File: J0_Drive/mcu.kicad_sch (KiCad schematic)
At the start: 1 part, among them U2 STM32G431RBTx

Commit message: started connecting root
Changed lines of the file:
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@@
 	(generator_version "10.0")
 	(paper "A4")
+	(wire
+		(pts
+			(xy 30.48 34.29) (xy 38.1 34.29)
+		)
+		(stroke
+			(width 0)
+			(type default)
+		)
+	)
+	(wire
+		(pts
+			(xy 30.48 39.37) (xy 38.1 39.37)
+		)
+		(stroke
+			(width 0)
+			(type default)
+		)
+	)
+	(wire
+		(pts
+			(xy 30.48 24.13) (xy 38.1 24.13)
+		)
+		(stroke
+			(width 0)
+			(type default)
+		)
+	)
+	(wire
+		(pts
+			(xy 30.48 21.59) (xy 38.1 21.59)
+		)
+		(stroke
+			(width 0)
+			(type default)
+		)
+	)
+	(wire
+		(pts
+			(xy 30.48 44.45) (xy 38.1 44.45)
+		)
+		(stroke
+			(width 0)
+			(type default)
+		)
+	)
+	(wire
+		(pts
+			(xy 30.48 46.99) (xy 38.1 46.99)
+		)
+		(stroke
+			(width 0)
+			(type default)
+		)
+	)
+	(wire
+		(pts
+			(xy 30.48 26.67) (xy 38.1 26.67)
+		)
+		(stroke
+			(width 0)
+			(type default)
+		)
+	)
+	(wire
+		(pts
+			(xy 30.48 31.75) (xy 38.1 31.75)
+		)
+		(stroke
+			(width 0)
+			(type default)
+		)
+	)
+	(wire
+		(pts
+			(xy 30.48 49.53) (xy 38.1 49.53)
+		)
+		(stroke
+			(width 0)
+			(type default)
+		)
+	)
+	(wire
+		(pts
+			(xy 30.48 29.21) (xy 38.1 29.21)
+		)
+		(stroke
+			(width 0)
+			(type default)
+		)
+	)
+	(label "ISENSE_C"
+		(at 38.1 49.53 0)
+		(effects
+			(font
+				(size 1.27 1.27)
+			)
+			(justify left bottom)
+		)
+	)
+	(label "INH3{slash}IN3"
+		(at 38.1 31.75 0)
+		(effects
+			(font
+				(size 1.27 1.27)
+			)
+			(justify left bottom)
+		)
+	)
+	(label "nFAULT"
+		(at 38.1 39.37 0)
+		(effects
+			(font
+				(size 1.27 1.27)
+			)
+			(justify left bottom)
+		)
+	)
+	(label "ISENSE_A"
+		(at 38.1 44.45 0)
+		(effects
+			(font
+				(size 1.27 1.27)
+			)
+			(justify left bottom)
+		)
+	)
+	(label "INH2{slash}IN2"
+		(at 38.1 26.67 0)
+		(effects
+			(font
+				(size 1.27 1.27)
+			)
+			(justify left bottom)
+		)
+	)
+	(label "INL1{slash}EN1"
+		(at 38.1 24.13 0)
+		(effects
+			(font
+				(size 1.27 1.27)
+			)
+			(justify left bottom)
+		)
+	)
+	(label "INH1{slash}IN1"
+		(at 38.1 21.59 0)
+		(effects
+			(font
+				(size 1.27 1.27)
+			)
+			(justify left bottom)
+		)
+	)
+	(label "INL2{slash}EN2"
+		(at 38.1 29.21 0)
+		(effects
+			(font
+				(size 1.27 1.27)
+			)
+			(justify left bottom)
+		)
+	)
+	(label "INL3{slash}EN3"
+		(at 38.1 34.29 0)
+		(effects
+			(font
+				(size 1.27 1.27)
+			)
+			(justify left bottom)
+		)
+	)
+	(label "ISENSE_B"
+		(at 38.1 46.99 0)
+		(effects
+			(font
+				(size 1.27 1.27)
+			)
+			(justify left bottom)
+		)
+	)
+	(hierarchical_label "ISENSE_A"
+		(shape input)
+		(at 30.48 44.45 180)
+		(effects
+			(font
+				(size 1.27 1.27)
+			)
+			(justify right)
+		)
+	)
 	(hierarchical_label "INL1{slash}EN1"
 		(shape output)
-		(at 105.41 82.55 180)
+		(at 30.48 24.13 180)
 		(effects
 			(font
@@
 	(hierarchical_label "nFAULT"
 		(shape input)
-		(at 102.87 101.6 180)
+		(at 30.48 39.37 180)
 		(effects
 			(font
@@
 	(hierarchical_label "INL3{slash}EN3"
 		(shape output)
-		(at 105.41 87.63 180)
+		(at 30.48 34.29 180)
+		(effects
+			(font
+				(size 1.27 1.27)
+			)
+			(justify right)
+		)
+	)
+	(hierarchical_label "ISENSE_C"
+		(shape input)
+		(at 30.48 49.53 180)
 		(effects
 			(font
@@
 	(hierarchical_label "INH3{slash}IN3"
 		(shape output)
-		(at 105.41 80.01 180)
+		(at 30.48 31.75 180)
 		(effects
 			(font
@@
 	(hierarchical_label "INH1{slash}IN1"
 		(shape output)
-		(at 105.41 74.93 180)
+		(at 30.48 21.59 180)
 		(effects
 			(font
@@
 	(hierarchical_label "INL2{slash}EN2"
 		(shape output)
-		(at 105.41 85.09 180)
+		(at 30.48 29.21 180)
+		(effects
+			(font
+				(size 1.27 1.27)
+			)
+			(justify right)
+		)
+	)
+	(hierarchical_label "ISENSE_B"
+		(shape input)
+		(at 30.48 46.99 180)
 		(effects
 			(font
@@
 	(hierarchical_label "INH2{slash}IN2"
 		(shape output)
-		(at 105.41 77.47 180)
-		(effects
-			(font
+		(at 30.48 26.67 180)
+		(effects
+			(font

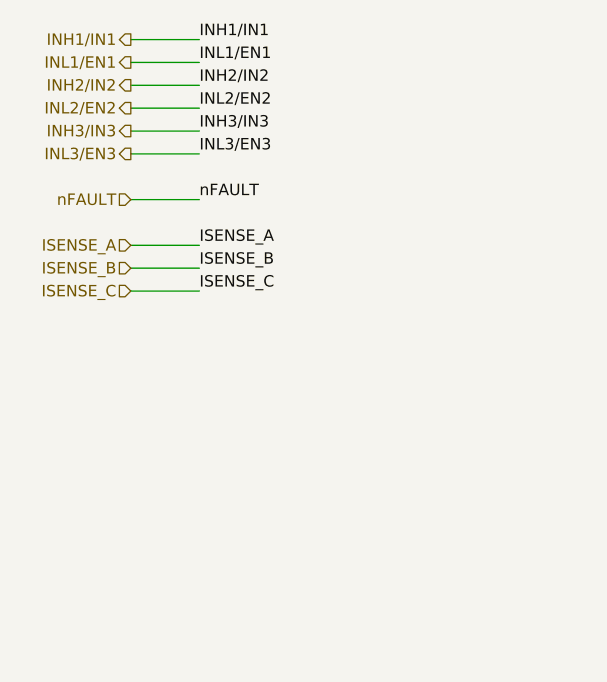
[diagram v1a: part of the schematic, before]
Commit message: organized hierarchical sheets, finished communications, started sensors
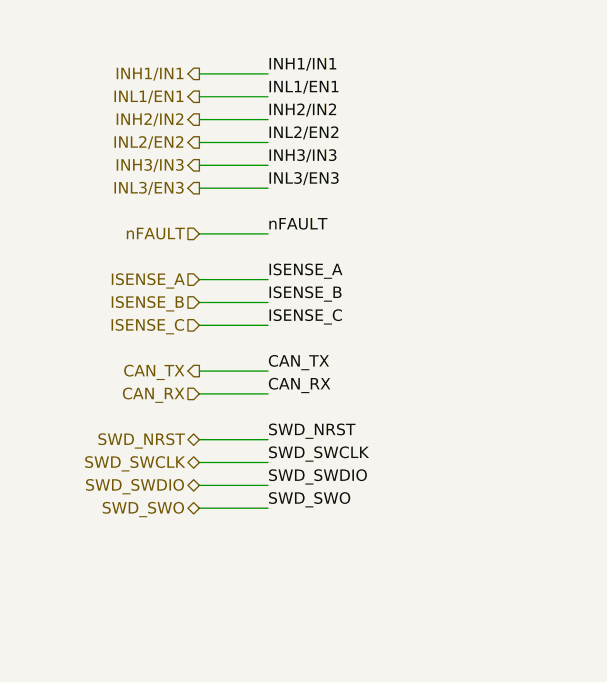
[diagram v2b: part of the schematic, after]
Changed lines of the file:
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@@
 	(wire
 		(pts
-			(xy 30.48 34.29) (xy 38.1 34.29)
-		)
-		(stroke
-			(width 0)
-			(type default)
-		)
-	)
-	(wire
-		(pts
-			(xy 30.48 39.37) (xy 38.1 39.37)
-		)
-		(stroke
-			(width 0)
-			(type default)
-		)
-	)
-	(wire
-		(pts
-			(xy 30.48 24.13) (xy 38.1 24.13)
-		)
-		(stroke
-			(width 0)
-			(type default)
-		)
-	)
-	(wire
-		(pts
-			(xy 30.48 21.59) (xy 38.1 21.59)
-		)
-		(stroke
-			(width 0)
-			(type default)
-		)
-	)
-	(wire
-		(pts
-			(xy 30.48 44.45) (xy 38.1 44.45)
-		)
-		(stroke
-			(width 0)
-			(type default)
-		)
-	)
-	(wire
-		(pts
-			(xy 30.48 46.99) (xy 38.1 46.99)
-		)
-		(stroke
-			(width 0)
-			(type default)
-		)
-	)
-	(wire
-		(pts
-			(xy 30.48 26.67) (xy 38.1 26.67)
-		)
-		(stroke
-			(width 0)
-			(type default)
-		)
-	)
-	(wire
-		(pts
-			(xy 30.48 31.75) (xy 38.1 31.75)
-		)
-		(stroke
-			(width 0)
-			(type default)
-		)
-	)
-	(wire
-		(pts
-			(xy 30.48 49.53) (xy 38.1 49.53)
-		)
-		(stroke
-			(width 0)
-			(type default)
-		)
-	)
-	(wire
-		(pts
-			(xy 30.48 29.21) (xy 38.1 29.21)
+			(xy 38.1 38.1) (xy 45.72 38.1)
+		)
+		(stroke
+			(width 0)
+			(type default)
+		)
+	)
+	(wire
+		(pts
+			(xy 38.1 43.18) (xy 45.72 43.18)
+		)
+		(stroke
+			(width 0)
+			(type default)
+		)
+	)
+	(wire
+		(pts
+			(xy 38.1 68.58) (xy 45.72 68.58)
+		)
+		(stroke
+			(width 0)
+			(type default)
+		)
+	)
+	(wire
+		(pts
+			(xy 38.1 66.04) (xy 45.72 66.04)
+		)
+		(stroke
+			(width 0)
+			(type default)
+		)
+	)
+	(wire
+		(pts
+			(xy 38.1 60.96) (xy 45.72 60.96)
+		)
+		(stroke
+			(width 0)
+			(type default)
+		)
+	)
+	(wire
+		(pts
+			(xy 38.1 73.66) (xy 45.72 73.66)
+		)
+		(stroke
+			(width 0)
+			(type default)
+		)
+	)
+	(wire
+		(pts
+			(xy 38.1 27.94) (xy 45.72 27.94)
+		)
+		(stroke
+			(width 0)
+			(type default)
+		)
+	)
+	(wire
+		(pts
+			(xy 38.1 25.4) (xy 45.72 25.4)
+		)
+		(stroke
+			(width 0)
+			(type default)
+		)
+	)
+	(wire
+		(pts
+			(xy 38.1 48.26) (xy 45.72 48.26)
+		)
+		(stroke
+			(width 0)
+			(type default)
+		)
+	)
+	(wire
+		(pts
+			(xy 38.1 50.8) (xy 45.72 50.8)
+		)
+		(stroke
+			(width 0)
+			(type default)
+		)
+	)
+	(wire
+		(pts
+			(xy 38.1 30.48) (xy 45.72 30.48)
+		)
+		(stroke
+			(width 0)
+			(type default)
+		)
+	)
+	(wire
+		(pts
+			(xy 38.1 71.12) (xy 45.72 71.12)
+		)
+		(stroke
+			(width 0)
+			(type default)
+		)
+	)
+	(wire
+		(pts
+			(xy 38.1 35.56) (xy 45.72 35.56)
+		)
+		(stroke
+			(width 0)
+			(type default)
+		)
+	)
+	(wire
+		(pts
+			(xy 38.1 53.34) (xy 45.72 53.34)
+		)
+		(stroke
+			(width 0)
+			(type default)
+		)
+	)
+	(wire
+		(pts
+			(xy 38.1 58.42) (xy 45.72 58.42)
+		)
+		(stroke
+			(width 0)
+			(type default)
+		)
+	)
+	(wire
+		(pts
+			(xy 38.1 33.02) (xy 45.72 33.02)
 		)
 		(stroke
@@
 	)
 	(label "ISENSE_C"
-		(at 38.1 49.53 0)
+		(at 45.72 53.34 0)
+		(effects
+			(font
+				(size 1.27 1.27)
+			)
+			(justify left bottom)
+		)
+	)
+	(label "SWD_SWDIO"
+		(at 45.72 71.12 0)
 		(effects
 			(font
@@
 	)
 	(label "INH3{slash}IN3"
-		(at 38.1 31.75 0)
+		(at 45.72 35.56 0)
+		(effects
+			(font
+				(size 1.27 1.27)
+			)
+			(justify left bottom)
+		)
+	)
+	(label "SWD_SWO"
+		(at 45.72 73.66 0)
+		(effects
+			(font
+				(size 1.27 1.27)
+			)
+			(justify left bottom)
+		)
+	)
+	(label "CAN_RX"
+		(at 45.72 60.96 0)
 		(effects
 			(font
@@
 	)
 	(label "nFAULT"
-		(at 38.1 39.37 0)
+		(at 45.72 43.18 0)
 		(effects
 			(font
@@
 	)
 	(label "ISENSE_A"
-		(at 38.1 44.45 0)
+		(at 45.72 48.26 0)
 		(effects
 			(font
@@
 	)
 	(label "INH2{slash}IN2"
-		(at 38.1 26.67 0)
+		(at 45.72 30.48 0)
 		(effects
 			(font
@@
 	)
 	(label "INL1{slash}EN1"
-		(at 38.1 24.13 0)
+		(at 45.72 27.94 0)
 		(effects
 			(font
@@
 	)
 	(label "INH1{slash}IN1"
-		(at 38.1 21.59 0)
+		(at 45.72 25.4 0)
 		(effects
 			(font
@@
 	)
 	(label "INL2{slash}EN2"
-		(at 38.1 29.21 0)
+		(at 45.72 33.02 0)
+		(effects
+			(font
+				(size 1.27 1.27)
+			)
+			(justify left bottom)
+		)
+	)
+	(label "CAN_TX"
+		(at 45.72 58.42 0)
 		(effects
 			(font
@@
 	)
 	(label "INL3{slash}EN3"
-		(at 38.1 34.29 0)
+		(at 45.72 38.1 0)
+		(effects
+			(font
+				(size 1.27 1.27)
+			)
+			(justify left bottom)
+		)
+	)
+	(label "SWD_SWCLK"
+		(at 45.72 68.58 0)
 		(effects
 			(font
@@
 	)
 	(label "ISENSE_B"
-		(at 38.1 46.99 0)
+		(at 45.72 50.8 0)
+		(effects
+			(font
+				(size 1.27 1.27)
+			)
+			(justify left bottom)
+		)
+	)
+	(label "SWD_NRST"
+		(at 45.72 66.04 0)
 		(effects
 			(font
@@
 	(hierarchical_label "ISENSE_A"
 		(shape input)
-		(at 30.48 44.45 180)
+		(at 38.1 48.26 180)
+		(effects
+			(font
+				(size 1.27 1.27)
+			)
+			(justify right)
+		)
+	)
+	(hierarchical_label "SWD_SWDIO"
+		(shape bidirectional)
+		(at 38.1 71.12 180)
 		(effects
 			(font
@@
 	(hierarchical_label "INL1{slash}EN1"
 		(shape output)
-		(at 30.48 24.13 180)
+		(at 38.1 27.94 180)
+		(effects
+			(font
+				(size 1.27 1.27)
+			)
+			(justify right)
+		)
+	)
+	(hierarchical_label "SWD_SWO"
+		(shape bidirectional)
+		(at 38.1 73.66 180)
 		(effects
 			(font
@@
 	(hierarchical_label "nFAULT"
 		(shape input)
-		(at 30.48 39.37 180)
+		(at 38.1 43.18 180)
+		(effects
+			(font
+				(size 1.27 1.27)
+			)
+			(justify right)
+		)
+	)
+	(hierarchical_label "CAN_TX"
+		(shape output)
+		(at 38.1 58.42 180)
 		(effects
 			(font
@@
 	(hierarchical_label "INL3{slash}EN3"
 		(shape output)
-		(at 30.48 34.29 180)
+		(at 38.1 38.1 180)
 		(effects
 			(font
@@
 	(hierarchical_label "ISENSE_C"
 		(shape input)
-		(at 30.48 49.53 180)
+		(at 38.1 53.34 180)
+		(effects
+			(font
+				(size 1.27 1.27)
+			)
+			(justify right)
+		)
+	)
+	(hierarchical_label "CAN_RX"
+		(shape input)
+		(at 38.1 60.96 180)
+		(effects
+			(font
+				(size 1.27 1.27)
+			)
+			(justify right)
+		)
+	)
+	(hierarchical_label "SWD_SWCLK"
+		(shape bidirectional)
+		(at 38.1 68.58 180)
 		(effects
 			(font
@@
 	(hierarchical_label "INH3{slash}IN3"
 		(shape output)
-		(at 30.48 31.75 180)
+		(at 38.1 35.56 180)
 		(effects
 			(font
@@
 	(hierarchical_label "INH1{slash}IN1"
 		(shape output)
-		(at 30.48 21.59 180)
+		(at 38.1 25.4 180)
 		(effects
 			(font
@@
 	(hierarchical_label "INL2{slash}EN2"
 		(shape output)
-		(at 30.48 29.21 180)
+		(at 38.1 33.02 180)
+		(effects
+			(font
+				(size 1.27 1.27)
+			)
+			(justify right)
+		)
+	)
+	(hierarchical_label "SWD_NRST"
+		(shape bidirectional)
+		(at 38.1 66.04 180)
 		(effects
 			(font
@@
 	(hierarchical_label "ISENSE_B"
 		(shape input)
-		(at 30.48 46.99 180)
+		(at 38.1 50.8 180)
 		(effects
 			(font
@@
 	(hierarchical_label "INH2{slash}IN2"
 		(shape output)
-		(at 30.48 26.67 180)
-		(effects
-			(font
+		(at 38.1 30.48 180)
+		(effects
+			(font

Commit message: started misc page, added test points, mounting holes, fiducials, etc.
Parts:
- added U8: LM5164DDA, Package_SO:HSOP-8-1EP_3.9x4.9mm_P1.27mm_EP2.41x3.1mm_ThermalVias, symbol Regulator_Switching:LM5164DDA
- added U9: TLV75533PDBV, Package_TO_SOT_SMD:SOT-23-5, symbol Regulator_Linear:TLV75533PDBV
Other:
- note added: "(follow typical application)"
- note added: "3.3V Regulator"
- note added: "5V Buck"
- note added: "5V to 3.3V"
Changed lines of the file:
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@@
 	(generator_version "10.0")
 	(paper "A4")
+	(text "5V to 3.3V"
+		(exclude_from_sim no)
+		(at 230.378 74.676 0)
+		(effects
+			(font
+				(size 1.27 1.27)
+			)
+			(justify left top)
+		)
+	)
+	(text "(follow typical application)"
+		(exclude_from_sim no)
+		(at 218.694 35.306 0)
+		(effects
+			(font
+				(size 1.27 1.27)
+			)
+			(justify left top)
+		)
+	)
+	(text "5V Buck"
+		(exclude_from_sim no)
+		(at 236.22 32.004 0)
+		(effects
+			(font
+				(size 1.27 1.27)
+			)
+			(justify left top)
+		)
+	)
+	(text "3.3V Regulator"
+		(exclude_from_sim no)
+		(at 230.124 72.39 0)
+		(effects
+			(font
+				(size 1.27 1.27)
+			)
+			(justify left top)
+		)
+	)
 	(wire
 		(pts
@@
 					(unit 1)
 				)
+			)
+		)
+	)
+	(symbol
+		(lib_id "Regulator_Switching:LM5164DDA")
+		(at 251.46 48.26 0)
+		(unit 1)
+		(body_style 1)
+		(exclude_from_sim no)
+		(in_bom yes)
+		(on_board yes)
+		(in_pos_files yes)
+		(dnp no)
+		(fields_autoplaced yes)
+		(property "Reference" "U8"
+			(at 251.46 33.02 0)
+			(show_name no)
+			(do_not_autoplace no)
+			(effects
+				(font
+					(size 1.27 1.27)
+				)
+			)
+		)
+		(property "Value" "LM5164DDA"
+			(at 251.46 35.56 0)
+			(show_name no)
+			(do_not_autoplace no)
+			(effects
+				(font
+					(size 1.27 1.27)
+				)
+			)
+		)
+		(property "Footprint" "Package_SO:HSOP-8-1EP_3.9x4.9mm_P1.27mm_EP2.41x3.1mm_ThermalVias"
+			(at 252.73 59.69 0)
+			(hide yes)
+			(show_name no)
+			(do_not_autoplace no)
+			(effects
+				(font
+					(size 1.27 1.27)
+				)
+			)
+		)
+		(property "Datasheet" "https://www.ti.com/lit/ds/symlink/lm5164.pdf?ts=1598311864250&ref_url=https%253A%252F%252Fwww.ti.com%252Fproduct%252FLM5164%253FHQS%253DTI-null-null-octopart-df-pf-null-wwe"
+			(at 243.84 39.37 0)
+			(hide yes)
+			(show_name no)
+			(do_not_autoplace no)
+			(effects
+				(font
+					(size 1.27 1.27)
+				)
+			)
+		)
+		(property "Description" "1A synchronous buck converter with ultra-low IQ, 6V - 100V input, adjustable output voltage, HSOP-8"
+			(at 251.46 48.26 0)
+			(hide yes)
+			(show_name no)
+			(do_not_autoplace no)
+			(effects
+				(font
+					(size 1.27 1.27)
+				)
+			)
+		)
+		(pin "4"
+		)
+		(pin "6"
+		)
+		(pin "5"
+		)
+		(pin "9"
+		)
+		(pin "8"
+		)
+		(pin "2"
+		)
+		(pin "1"
+		)
+		(pin "7"
+		)
+		(pin "3"
+		)
+		(instances
+			(project "J0_Drive"
+				(path "/00bb46ee-9cfb-4ad9-9820-c6d5e19a8f16/7a7182ae-bba0-4f61-9325-38949d0b1394"
+					(reference "U8")
+					(unit 1)
+				)
+			)
+		)
+	)
+	(symbol
+		(lib_id "Regulator_Linear:TLV75533PDBV")
+		(at 248.92 86.36 0)
+		(unit 1)
+		(body_style 1)
+		(exclude_from_sim no)
+		(in_bom yes)
+		(on_board yes)
+		(in_pos_files yes)
+		(dnp no)
+		(fields_autoplaced yes)
+		(property "Reference" "U9"
+			(at 248.92 77.47 0)
+			(show_name no)
+			(do_not_autoplace no)
+			(effects
+				(font
+					(size 1.27 1.27)
+				)
+			)
+		)
+		(property "Value" "TLV75533PDBV"
+			(at 248.92 80.01 0)
+			(show_name no)
+			(do_not_autoplace no)
+			(effects
+				(font
+					(size 1.27 1.27)
+				)
+			)
+		)
+		(property "Footprint" "Package_TO_SOT_SMD:SOT-23-5"
+			(at 248.92 78.105 0)
+			(hide yes)
+			(show_name no)
+			(do_not_autoplace no)
+			(effects
+				(font
+					(size 1.27 1.27)
+					(italic yes)
+				)
+			)
+		)
+		(property "Datasheet" "http://www.ti.com/lit/ds/symlink/tlv755p.pdf"
+			(at 248.92 85.09 0)
+			(hide yes)
+			(show_name no)
+			(do_not_autoplace no)
+			(effects
+				(font
+					(size 1.27 1.27)
+				)
+			)
+		)
+		(property "Description" "500mA Low Dropout Voltage Regulator, Fixed Output 3.3V, SOT-23-5"
+			(at 248.92 86.36 0)
+			(hide yes)
+			(show_name no)
+			(do_not_autoplace no)
+			(effects
+				(font
+					(size 1.27 1.27)
+				)
+			)
+		)
+		(pin "2"
+		)
+		(pin "4"
+		)
+		(pin "3"
+		)
+		(pin "1"
+		)
+		(pin "5"
+		)
+		(instances
+			(project "J0_Drive"
+				(path "/00bb46ee-9cfb-4ad9-9820-c6d5e19a8f16/7a7182ae-bba0-4f61-9325-38949d0b1394"
+					(reference "U9")
+					(unit 1)
+				)
